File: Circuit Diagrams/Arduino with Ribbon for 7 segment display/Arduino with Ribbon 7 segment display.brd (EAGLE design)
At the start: 42.9 x 30.5 mm, 2 parts

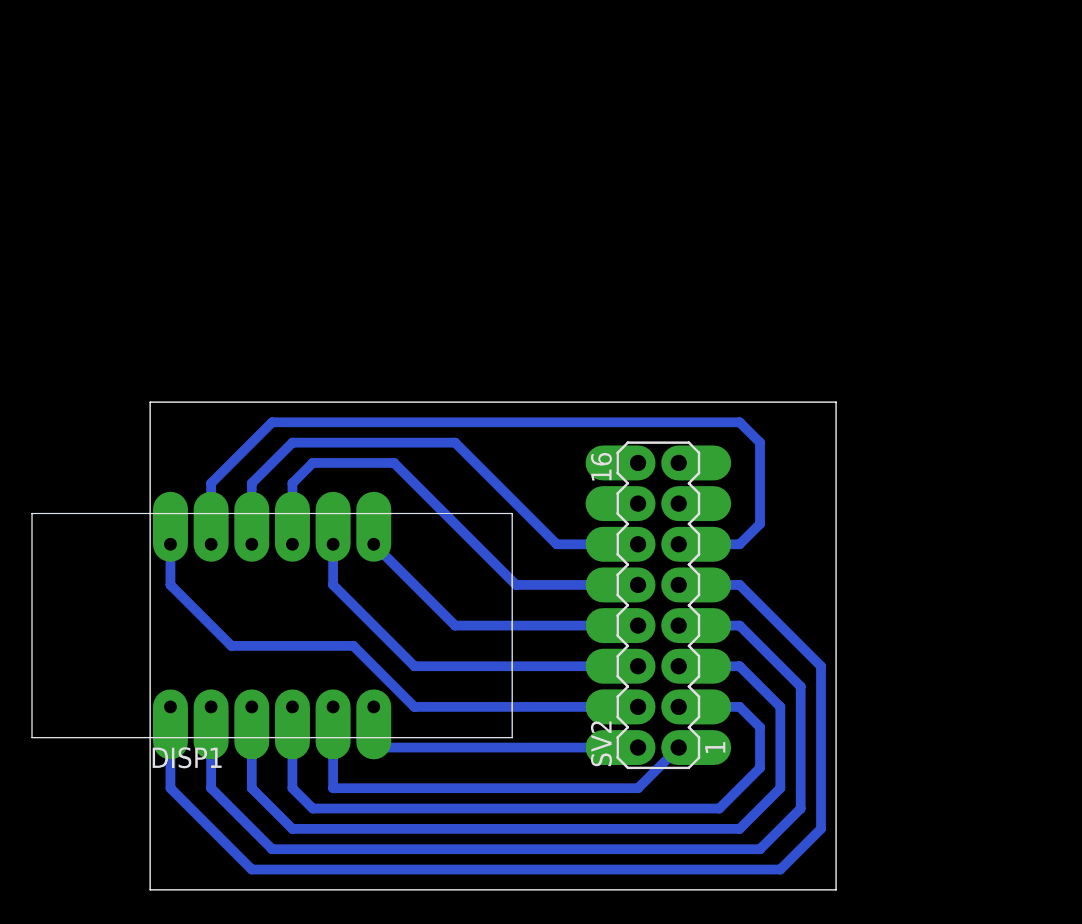
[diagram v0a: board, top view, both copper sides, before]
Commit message: Added electronics and 3d print designs.
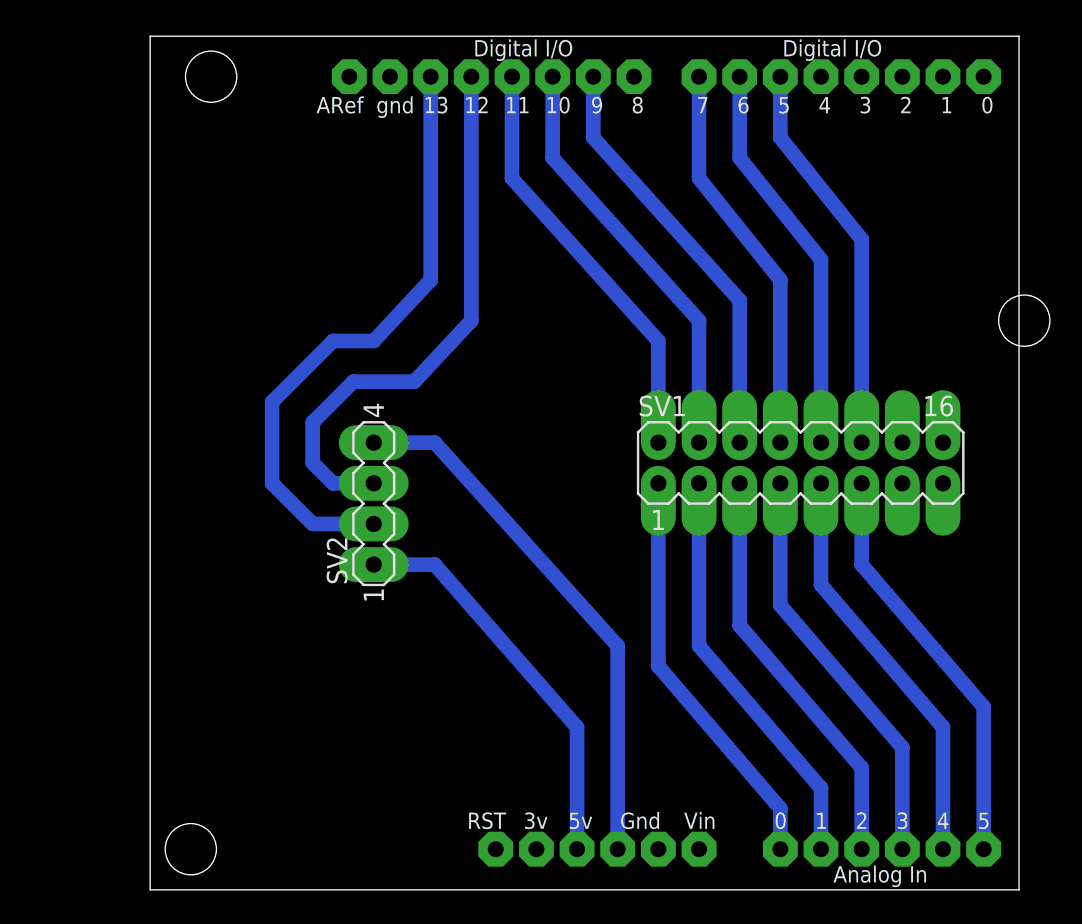
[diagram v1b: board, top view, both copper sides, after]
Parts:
- removed DISP1: 7-SEG_4D_0.36, 7-seg_disp_0.36in:7SEG-4DIG
- added SV1: (no value), con-lstb:MA08-2
- added U$1: ARDUINO-BPLACE, adafruit:ARDUINO-BPLACE
- SV2: device con-lstb:MA08-2 -> con-lstb:MA04-1
- moved SV2 18.9 mm to (14.0, 24.1)
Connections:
- new net 3V: U$1.3V
- new net GND: U$1.GND
- new net GND1: U$1.GND1
- new net N$13: SV2.4, U$1.GND2
- new net N$14: SV2.1, U$1.5V
- new net N$15: SV2.3, U$1.D12
- new net N$16: SV2.2, U$1.D13
- new net VIN: U$1.VIN
- net N$1: now also SV1.2, U$1.D11; no longer DISP1.C, SV2.3
- net N$10: now also SV1.7, U$1.A3; no longer DISP1.G, SV2.1
- net N$11: now also SV1.9, U$1.A4; no longer DISP1.F, SV2.12
- net N$12: now also SV1.11, U$1.A5; no longer DISP1.D, SV2.7
- net N$2: now also SV1.4, U$1.D10; no longer DISP1.D4, SV2.2
- net N$3: now also SV1.6, U$1.D9; no longer DISP1.D1, SV2.4
- net N$4: now also SV1.8, U$1.D7; no longer DISP1.D2, SV2.10
- net N$5: now also SV1.10, U$1.D6; no longer DISP1.D3, SV2.6
- net N$6: now also SV1.12, U$1.D5; no longer DISP1.DP, SV2.5
- net N$7: now also SV1.1, U$1.A0; no longer DISP1.B, SV2.8
- net N$8: now also SV1.3, U$1.A1; no longer DISP1.A, SV2.11
- net N$9: now also SV1.5, U$1.A2; no longer DISP1.E, SV2.9
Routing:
- net N$9: track 70.0 -> 25.7 mm
- net N$16: track 0.00 -> 38.3 mm
- net N$12: track 61.4 -> 25.7 mm
- net N$15: track 0.00 -> 34.7 mm
- net N$13: track 0.00 -> 33.6 mm
- net N$6: track 52.7 -> 24.6 mm
- net N$8: track 50.9 -> 25.7 mm
- net N$14: track 0.00 -> 24.9 mm
- net N$1: track 44.0 -> 26.4 mm
- net N$3: track 34.9 -> 26.4 mm
- net N$2: track 19.0 -> 26.4 mm
- net N$7: track 18.6 -> 25.7 mm
- net N$11: track 31.6 -> 25.7 mm
- net N$4: track 29.1 -> 24.6 mm
- net N$10: track 27.7 -> 25.7 mm
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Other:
- board size 42.9 x 30.5 mm -> 54.3 x 53.3 mm
